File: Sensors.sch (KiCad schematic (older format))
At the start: 10 parts, among them U1 MPU-9250

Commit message: Added in Buzzer and N channel mosfet
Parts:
- TP3, TP4, TP5: footprint TestPoint:TestPoint_Plated_Hole_D3.0mm -> TestPoint:TestPoint_Pad_1.0x1.0mm
- TP7: footprint (none) -> TestPoint:TestPoint_Pad_1.0x1.0mm
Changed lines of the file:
@@
 F 0 "TP5" V 1954 2238 50  0000 L CNN
 F 1 "TestPoint" V 2045 2238 50  0000 L CNN
-F 2 "TestPoint:TestPoint_Plated_Hole_D3.0mm" H 2200 2050 50  0001 C CNN
+F 2 "TestPoint:TestPoint_Pad_1.0x1.0mm" H 2200 2050 50  0001 C CNN
 F 3 "~" H 2200 2050 50  0001 C CNN
 	1    2000 2050
@@
 F 0 "TP4" V 1954 2038 50  0000 L CNN
 F 1 "TestPoint" V 2045 2038 50  0000 L CNN
-F 2 "TestPoint:TestPoint_Plated_Hole_D3.0mm" H 2200 1850 50  0001 C CNN
+F 2 "TestPoint:TestPoint_Pad_1.0x1.0mm" H 2200 1850 50  0001 C CNN
 F 3 "~" H 2200 1850 50  0001 C CNN
 	1    2000 1850
@@
 F 0 "TP3" V 1954 1888 50  0000 L CNN
 F 1 "TestPoint" V 2045 1888 50  0000 L CNN
-F 2 "TestPoint:TestPoint_Plated_Hole_D3.0mm" H 2200 1700 50  0001 C CNN
+F 2 "TestPoint:TestPoint_Pad_1.0x1.0mm" H 2200 1700 50  0001 C CNN
 F 3 "~" H 2200 1700 50  0001 C CNN
 	1    2000 1700
@@
 F 0 "TP7" V 1954 2438 50  0000 L CNN
 F 1 "TestPoint" V 2045 2438 50  0000 L CNN
-F 2 "" H 2200 2250 50  0001 C CNN
+F 2 "TestPoint:TestPoint_Pad_1.0x1.0mm" H 2200 2250 50  0001 C CNN
 F 3 "~" H 2200 2250 50  0001 C CNN
 	1    2000 2250

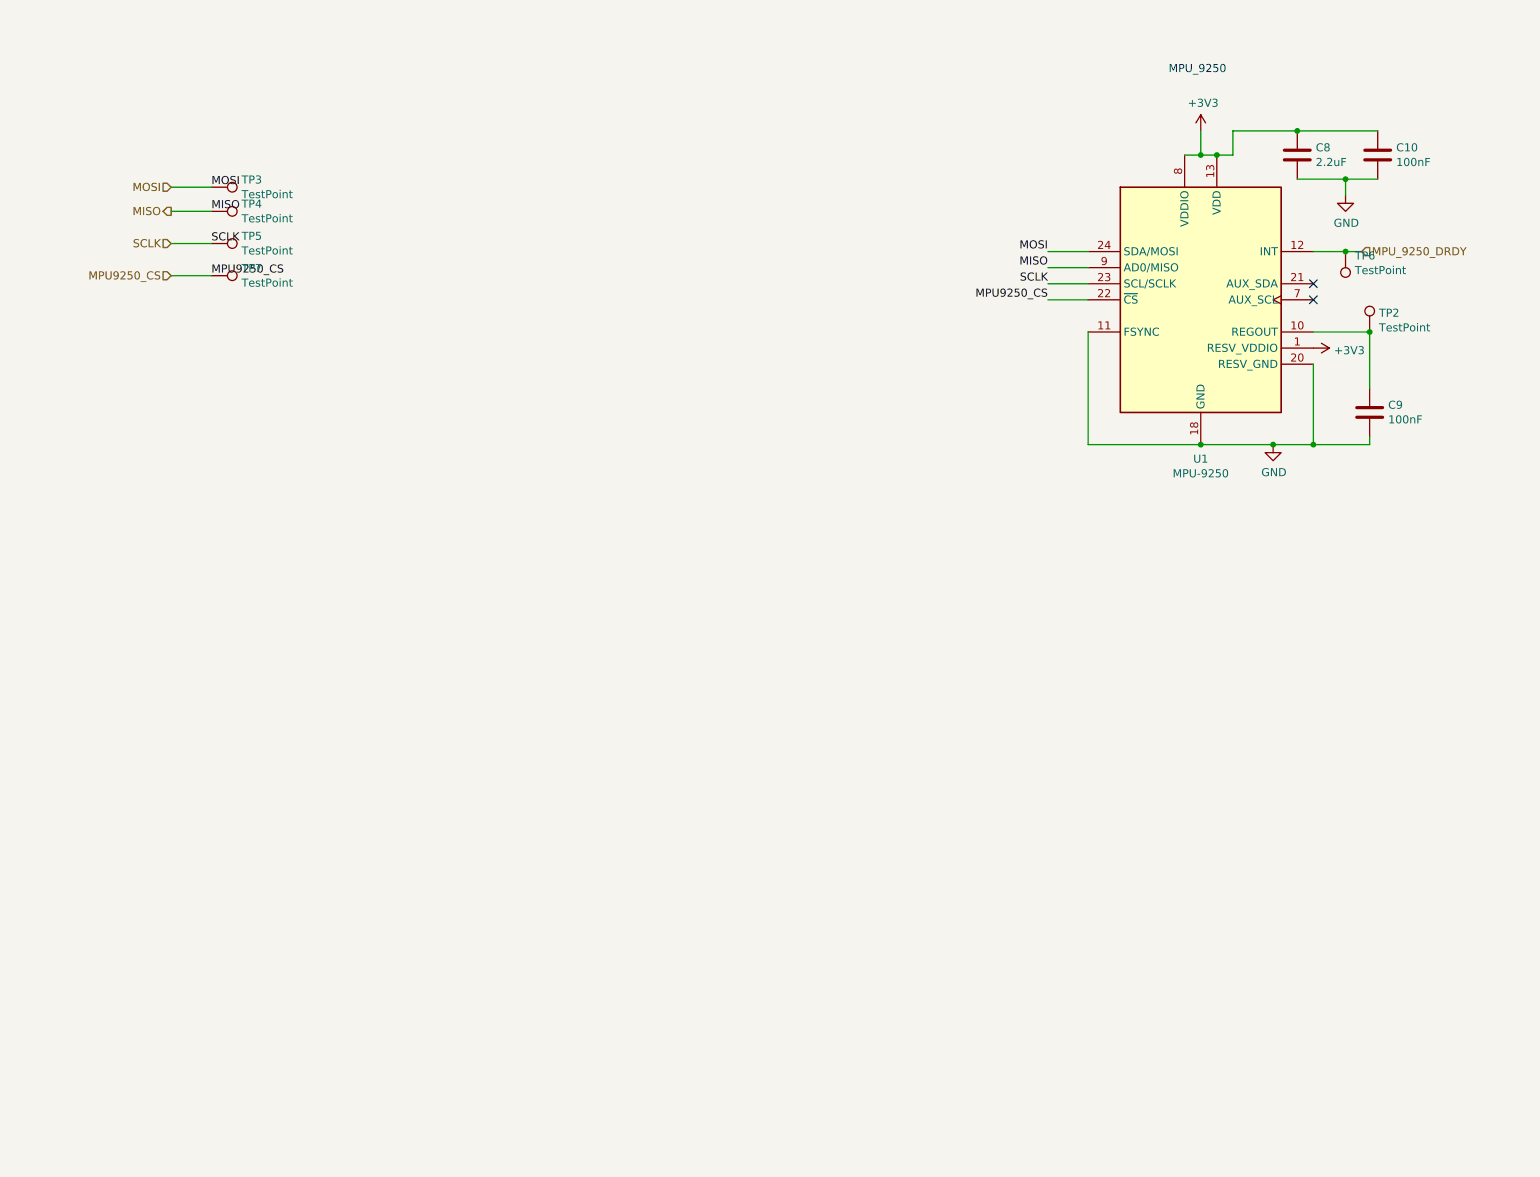
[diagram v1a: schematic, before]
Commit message: IMU1/2 added in plus regs
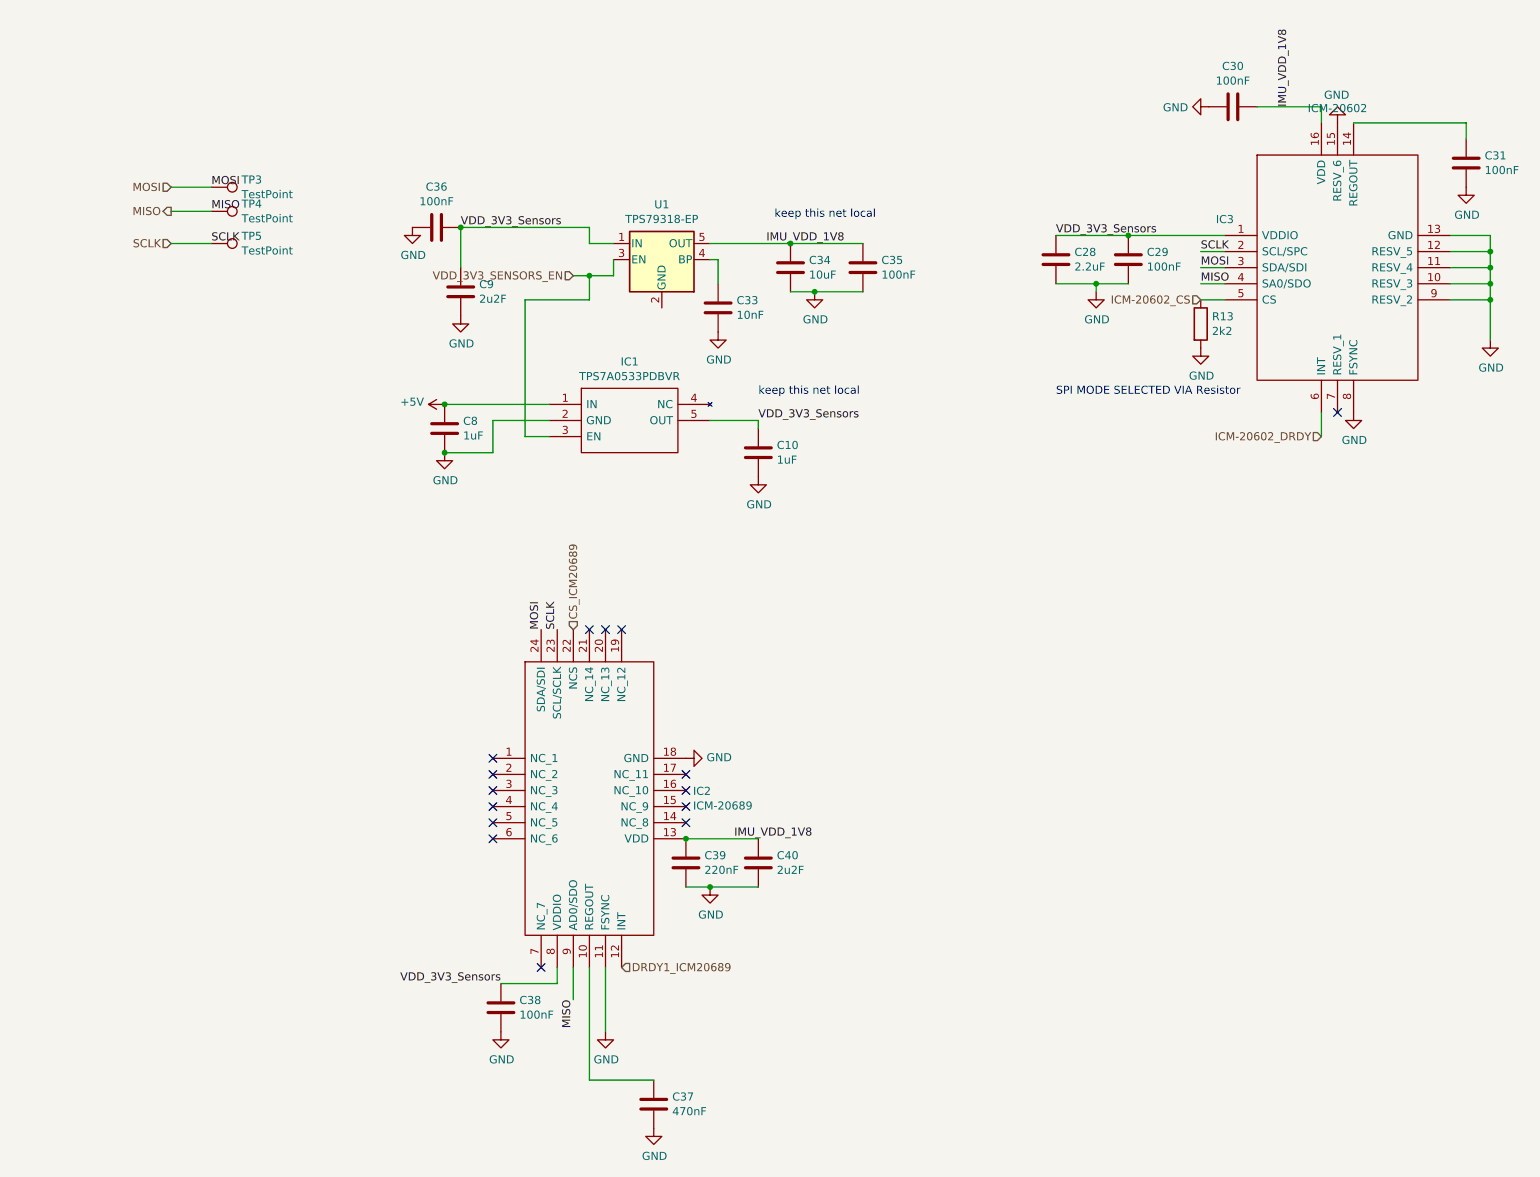
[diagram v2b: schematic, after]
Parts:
- removed TP2, TP6: TestPoint, TestPoint:TestPoint_Plated_Hole_D3.0mm, symbol Connector:TestPoint
- removed TP7: TestPoint, TestPoint:TestPoint_Pad_1.0x1.0mm, symbol Connector:TestPoint
- removed U1: MPU-9250, Sensor_Motion:InvenSense_QFN-24_3x3mm_P0.4mm, symbol Sensor_Motion:MPU-9250
- added C28: 2.2uF, symbol Device:C
- added C29: 100nF, Capacitor_SMD:C_0603_1608Metric_Pad1.05x0.95mm_HandSolder, symbol Device:C
- added C30, C31, C35, C36, C38: 100nF, symbol Device:C
- added C33: 10nF, symbol Device:C
- added C34: 10uF, symbol Device:C
- added C37: 470nF, symbol Device:C
- added C39: 220nF, symbol Device:C
- added C40: 2u2F, symbol Device:C
- added IC1: TPS7A0533PDBVR, SOT95P280X145-5N, symbol SamacSys_Parts:TPS7A0533PDBVR
- added IC2: ICM-20689, ICM20689, symbol SamacSys_Parts:ICM-20689
- added IC3: ICM-20602, PULL-BACK-QFN-16, symbol SamacSys_Parts:ICM-20602
- added R13: 2k2, Capacitor_SMD:C_0603_1608Metric_Pad1.05x0.95mm_HandSolder, symbol Device:R
- added U1: TPS79318-EP, Package_TO_SOT_SMD:SOT-23-5, symbol Regulator_Linear:TPS79318-EP
- C10: value 100nF -> 1uF; footprint Capacitor_SMD:C_0603_1608Metric_Pad1.05x0.95mm_HandSolder -> (none)
- C8: value 2.2uF -> 1uF
- C9: value 100nF -> 2u2F; footprint Capacitor_SMD:C_0603_1608Metric_Pad1.05x0.95mm_HandSolder -> (none)
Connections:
- net GND: now also C28.2, C29.2, C30.1, C31.2, C33.2, C34.2, C35.2, C36.2, C37.2, C38.2, C39.2, C40.2, IC1.2 (GND), IC2.11 (FSYNC), IC2.18 (GND), IC3.10 (RESV_3), IC3.11 (RESV_4), IC3.12 (RESV_5), IC3.13 (GND), IC3.15 (RESV_6), IC3.8 (FSYNC), IC3.9 (RESV_2), R13.2
- net MISO: now also IC2.9 (AD0/SDO), IC3.4 (SA0/SDO)
- net MOSI: now also IC2.24 (SDA/SDI), IC3.3 (SDA/SDI)
- net SCLK: now also IC2.23 (SCL/SCLK), IC3.2 (SCL/SPC)
- net VDD_3V3_Sensors: now reaches C9.1
- net VDD_3V3_Sensors: now also C10.1, C28.1, C29.1, C36.1, C38.1, IC1.5 (OUT), IC2.8 (VDDIO), IC3.1 (VDDIO), U1.1 (IN)
- net +3V3 renamed +5V
- net +5V: now also IC1.1 (IN); no longer C10.1
- new net: C31.1, IC3.14 (REGOUT)
- new net: C33.1, U1.4 (BP)
- new net: C37.1, IC2.10 (REGOUT)
- new net CS_ICM20689: IC2.22 (NCS)
- new net DRDY1_ICM20689: IC2.12 (INT)
- new net ICM-20602_CS: IC3.5 (CS), R13.1
- new net ICM-20602_DRDY: IC3.6 (INT)
- new net IMU_VDD_1V8: C30.2, C34.1, C35.1, C39.1, C40.1, IC2.13 (VDD), IC3.16 (VDD), U1.5 (OUT)
- new net VDD_3V3_SENSORS_EN: IC1.3 (EN), U1.3 (EN)
- no-connect marks 2 -> 15
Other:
- note added: "SPI MODE SELECTED VIA Resistor\n"
- note added: "keep this net local\n"
- note removed: "MPU_9250\n"

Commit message: Added in Magnetometer and barometer
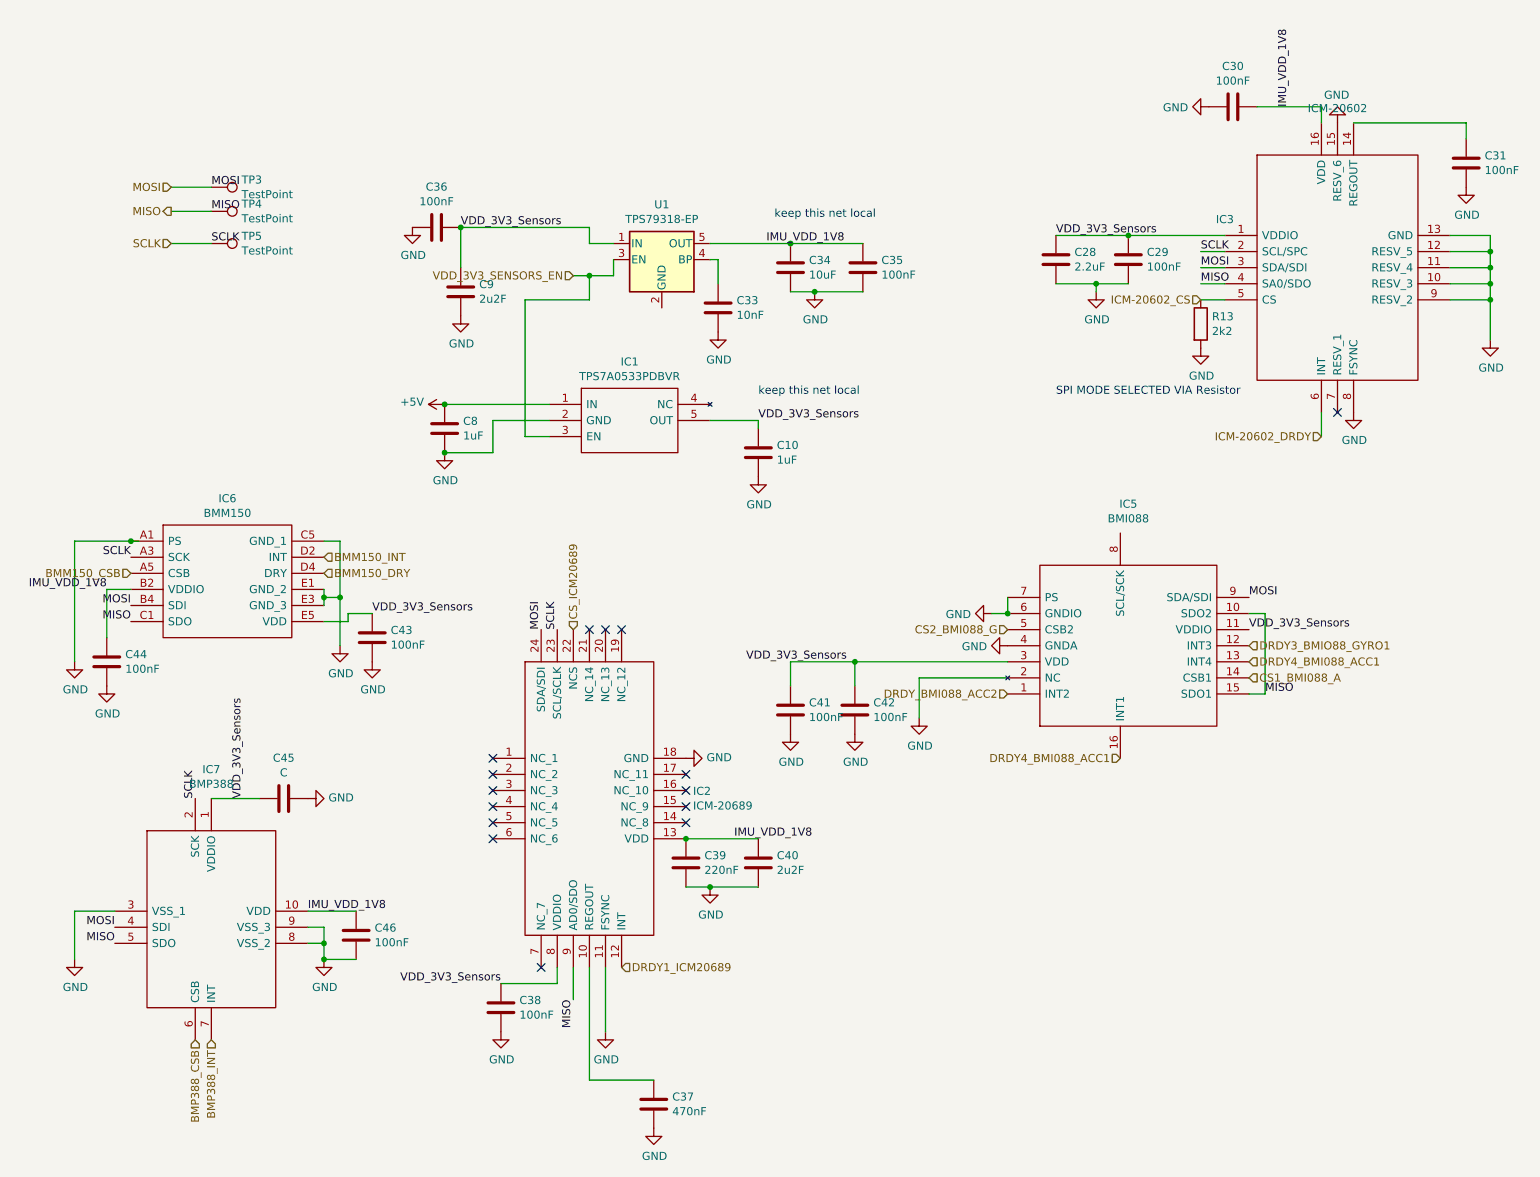
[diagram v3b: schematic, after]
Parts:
- added C41, C42, C43, C44, C46: 100nF, Capacitor_SMD:C_0603_1608Metric_Pad1.05x0.95mm_HandSolder, symbol Device:C
- added C45: C, symbol Device:C
- added IC5: BMI088, BMI088, symbol SamacSys_Parts:BMI088
- added IC6: BMM150, BGA12C28P5X5_156X156X40, symbol SamacSys_Parts:BMM150
- added IC7: BMP388, BMP388, symbol SamacSys_Parts:BMP388
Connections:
- net GND: now also C41.2, C42.2, C43.2, C44.2, C45.1, C46.2, IC5.2 (NC), IC5.4 (GNDA), IC5.6 (GNDIO), IC5.7 (PS), IC6.A1 (PS), IC6.C5 (GND_1), IC6.E1 (GND_2), IC6.E3 (GND_3), IC7.3 (VSS_1), IC7.8 (VSS_2), IC7.9 (VSS_3)
- net IMU_VDD_1V8: now also C44.1, C46.1, IC6.B2 (VDDIO), IC7.10 (VDD)
- net MISO: now also IC5.10 (SDO2), IC5.15 (SDO1), IC6.C1 (SDO), IC7.5 (SDO)
- net MOSI: now also IC5.9 (SDA/SDI), IC6.B4 (SDI), IC7.4 (SDI)
- net SCLK: now also IC6.A3 (SCK), IC7.2 (SCK)
- net VDD_3V3_Sensors: now also C41.1, C42.1, C43.1, C45.2, IC5.11 (VDDIO), IC5.3 (VDD), IC6.E5 (VDD), IC7.1 (VDDIO)
- new net BMM150_CSB: IC6.A5 (CSB)
- new net BMM150_DRY: IC6.D4 (DRY)
- new net BMM150_INT: IC6.D2 (INT)
- new net BMP388_CSB: IC7.6 (CSB)
- new net BMP388_INT: IC7.7 (INT)
- new net CS1_BMI088_A: IC5.14 (CSB1)
- new net CS2_BMI088_G: IC5.5 (CSB2)
- new net DRDY3_BMIO88_GYRO1: IC5.12 (INT3)
- new net DRDY4_BMI088_ACC1: IC5.13 (INT4), IC5.16 (INT1)
- new net DRDY_BMI088_ACC2: IC5.1 (INT2)
